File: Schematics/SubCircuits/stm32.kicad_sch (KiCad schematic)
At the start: 16 parts, among them J10 MainBoard, J11 O, J7 I, J8 I2C_OLED, J9 Prog edge, SW2 RST, U5 STM32G070K

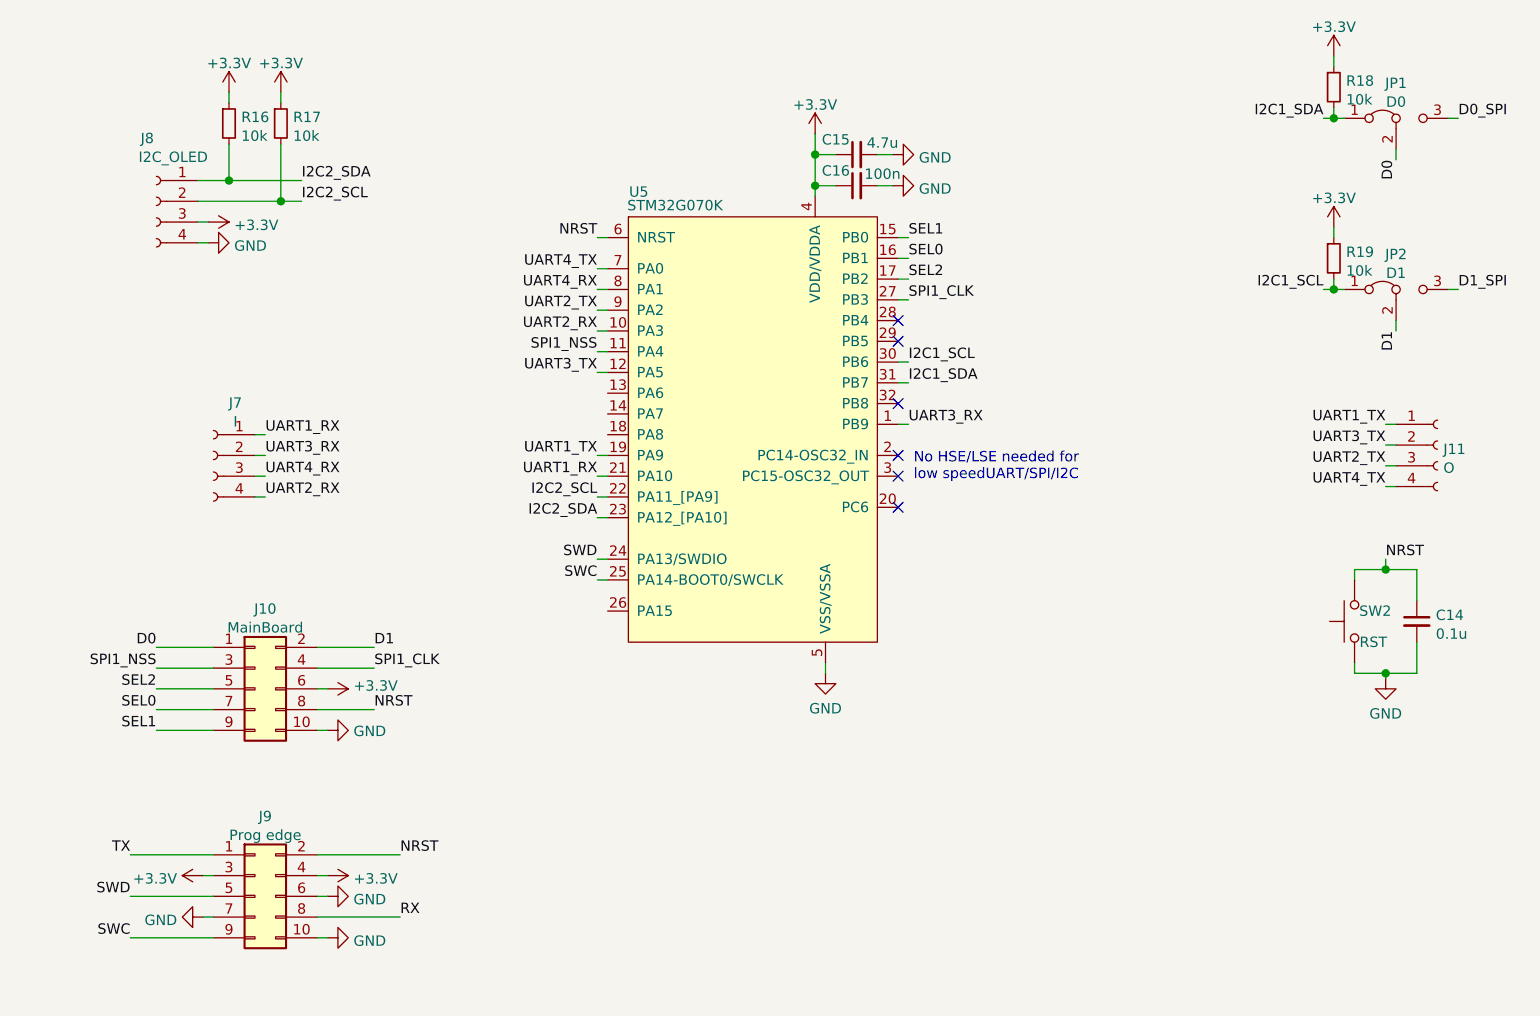
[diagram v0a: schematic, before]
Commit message: Added defunct subcircuit project
superseded by modular mainboard
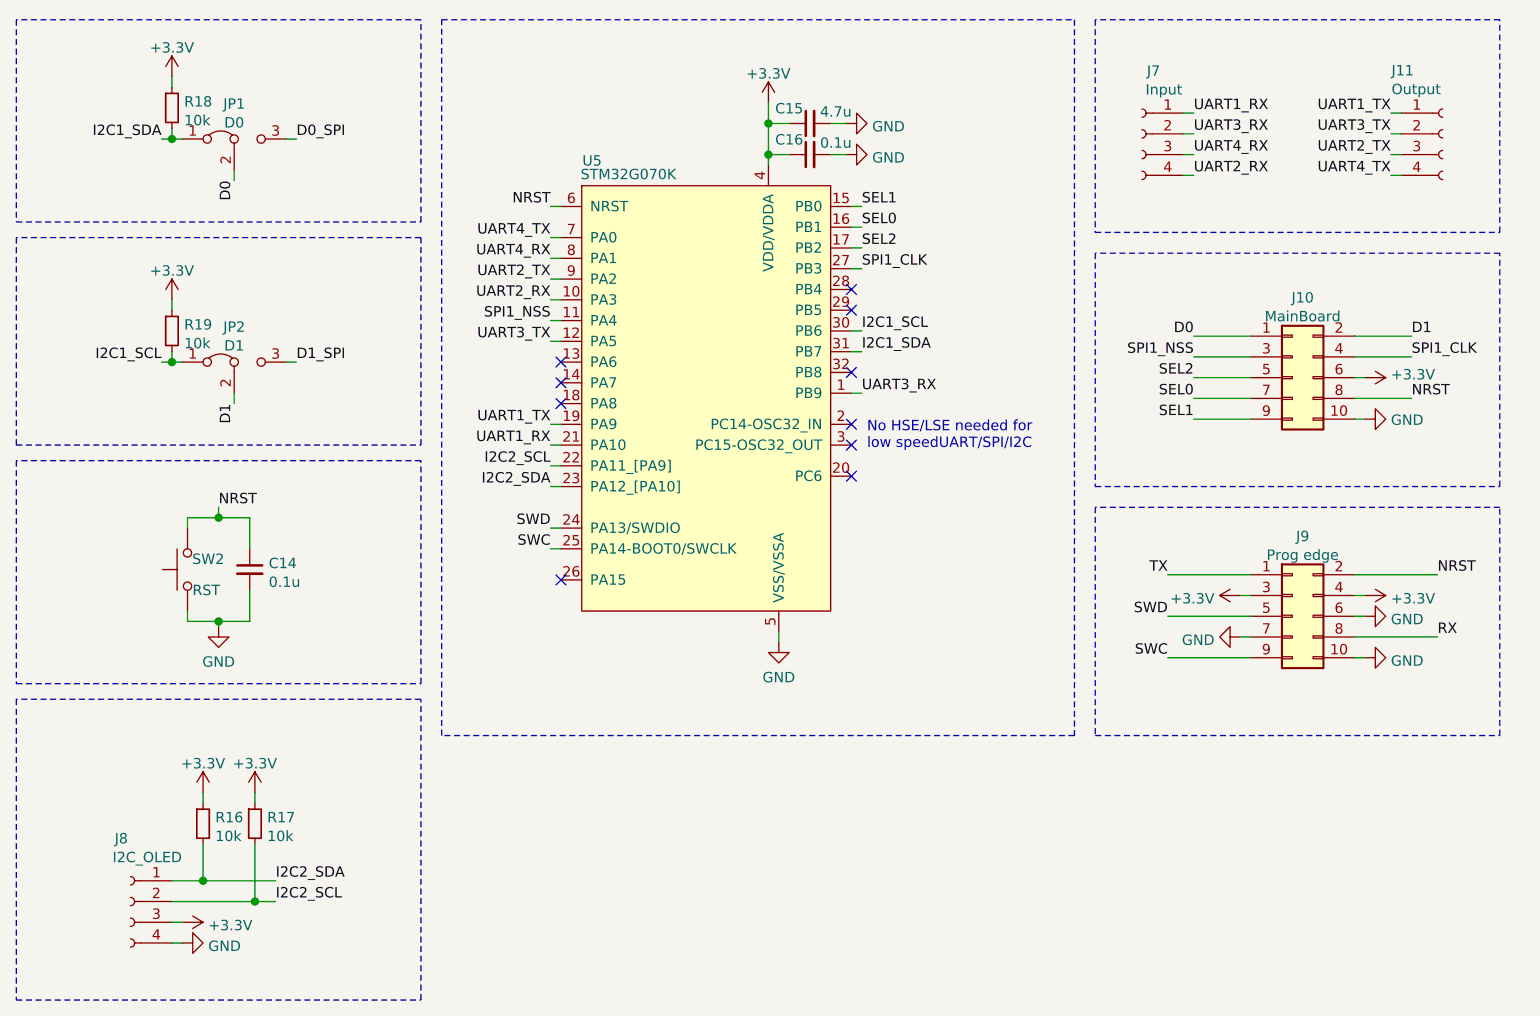
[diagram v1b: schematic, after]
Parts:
- C15: LCSC Part (none) -> C19666
- C16: value 100n -> 0.1u; LCSC Part (none) -> C14663
- J11: value O -> Output
- J7: value I -> Input
- SW2: LCSC Part (none) -> C115357
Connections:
- no-connect marks 6 -> 10
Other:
- moved on the sheet: C14, C15, C16, J10, J11, J7, J8, J9, JP1, JP2, R16, R17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
